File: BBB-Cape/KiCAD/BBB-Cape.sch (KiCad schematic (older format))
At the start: 0 parts

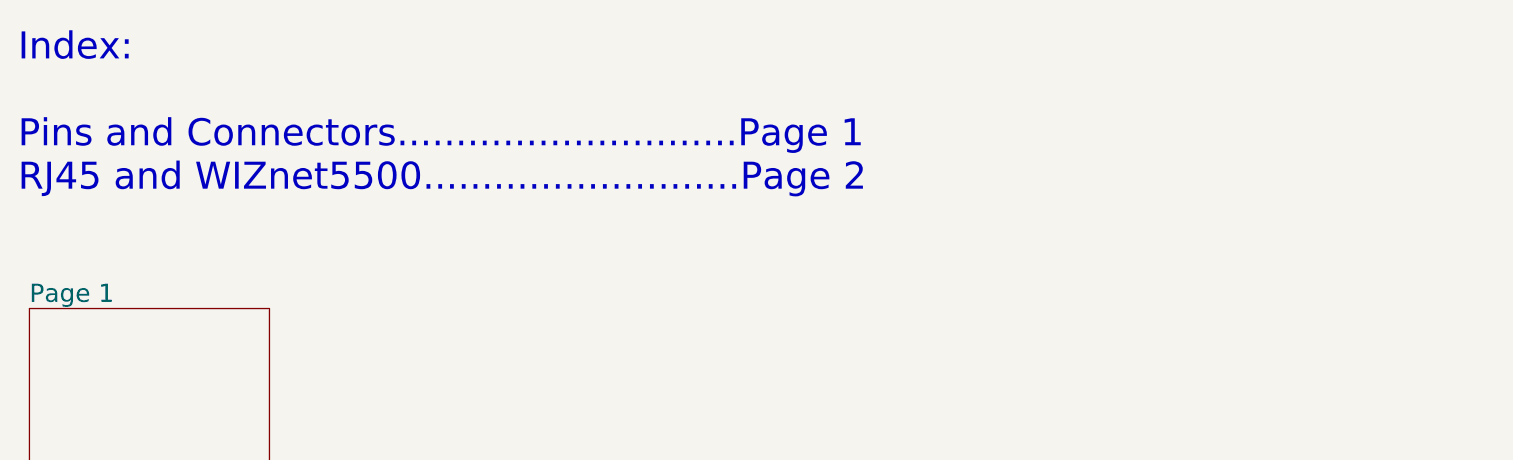
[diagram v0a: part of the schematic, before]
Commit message: layout reorganzied, before SMD molex
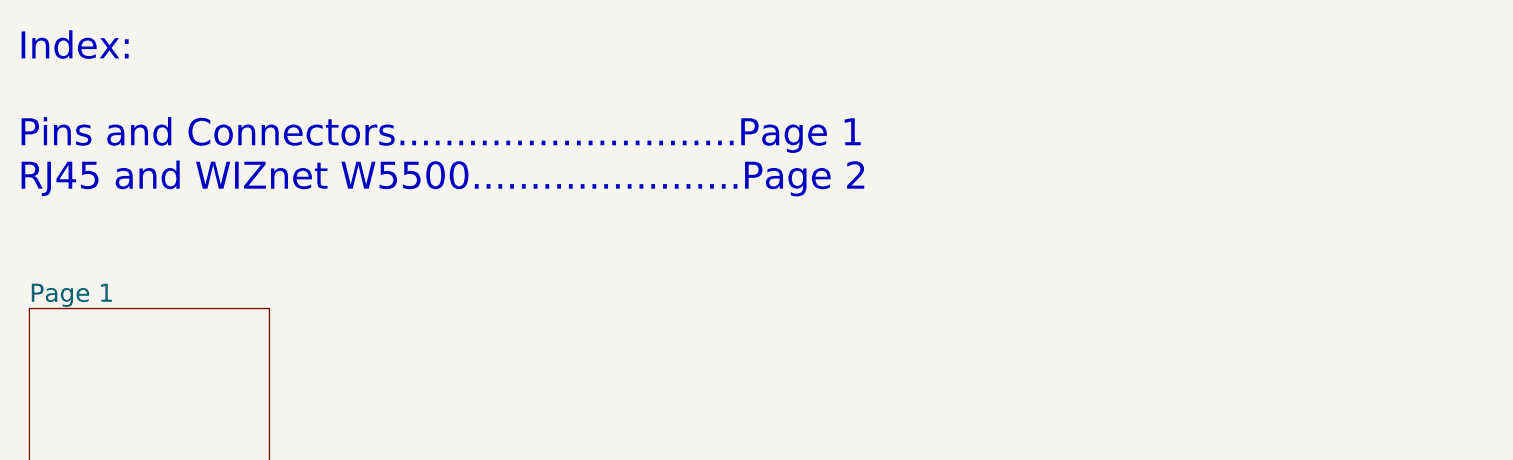
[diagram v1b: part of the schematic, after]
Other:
- note added: "Index:\n\nPins and Connectors.............................Page 1\nRJ45 and WIZnet W5500.......................Page 2"
- note removed: "Index:\n\nPins and Connectors.............................Page 1\nRJ45 and WIZnet5500...........................Page 2"
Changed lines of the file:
@@
 LIBS:atmel
 LIBS:contrib
+LIBS:Switch
 LIBS:valves
 LIBS:WIZnet_W5500_MagJack-cache
@@
 $EndDescr
 Text Notes 1200 2250 0    118  ~ 0
-Index:\n\nPins and Connectors.............................Page 1\nRJ45 and WIZnet5500...........................Page 2
+Index:\n\nPins and Connectors.............................Page 1\nRJ45 and WIZnet W5500.......................Page 2
 $Sheet
 S 1250 2750 1050 900
